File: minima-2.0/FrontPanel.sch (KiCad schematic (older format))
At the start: 41 parts

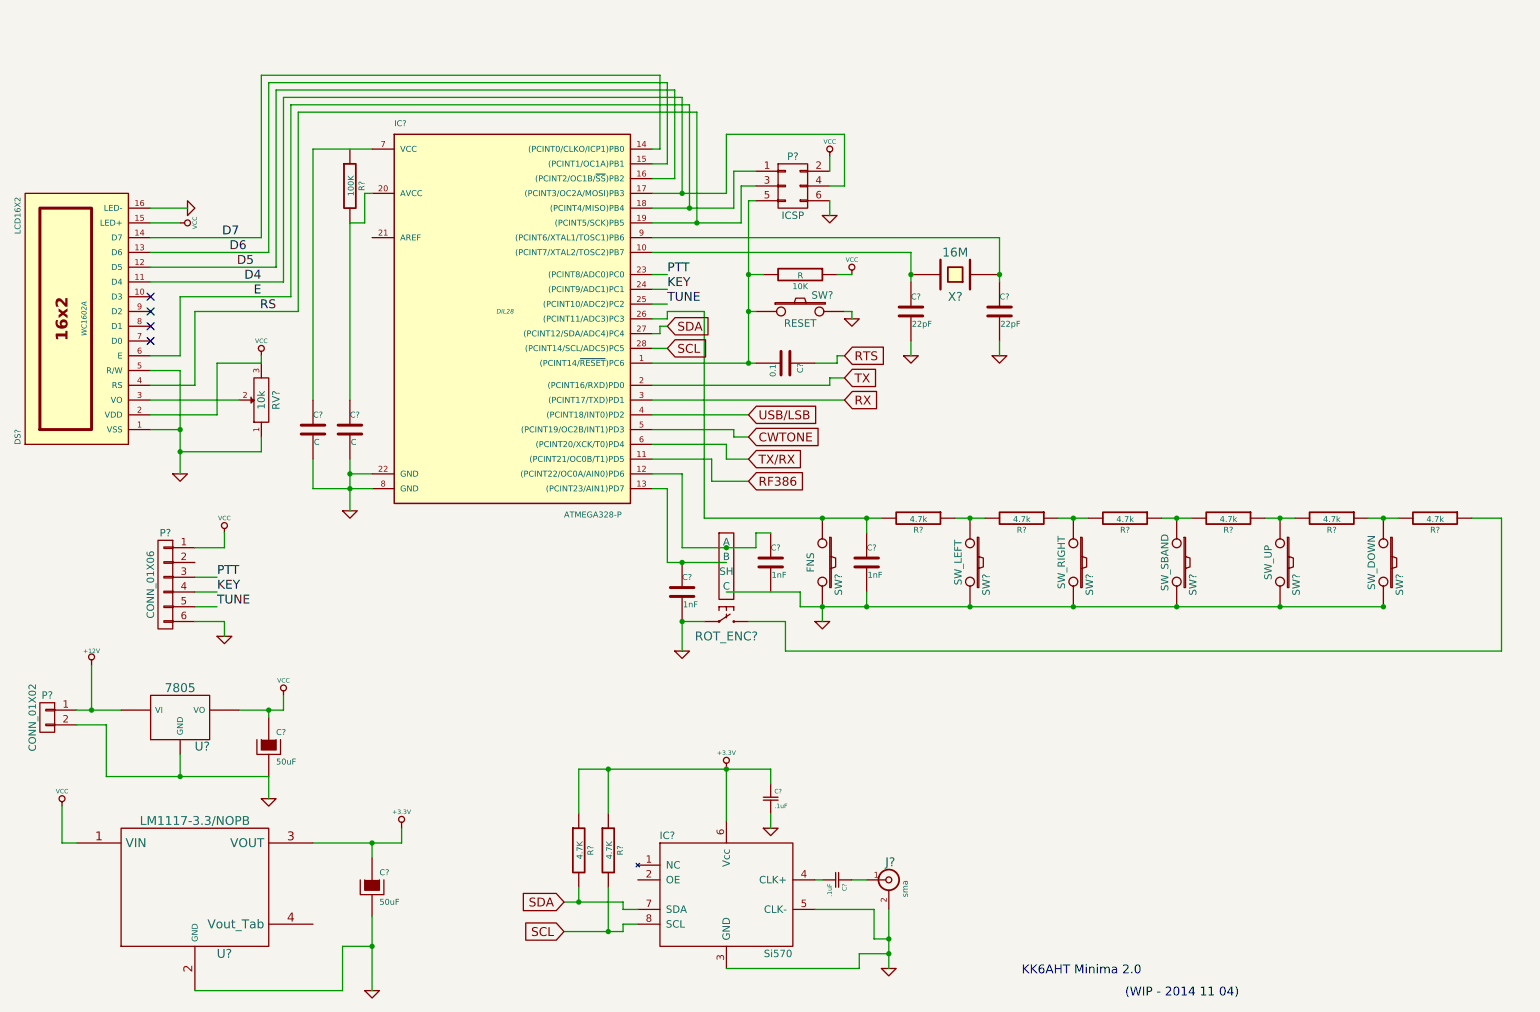
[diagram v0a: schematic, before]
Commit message: Finishing touches on schematic
 - Added missing 47k on AREF
 - Added connectors for all outside connections
 - Fixed all ERC errors
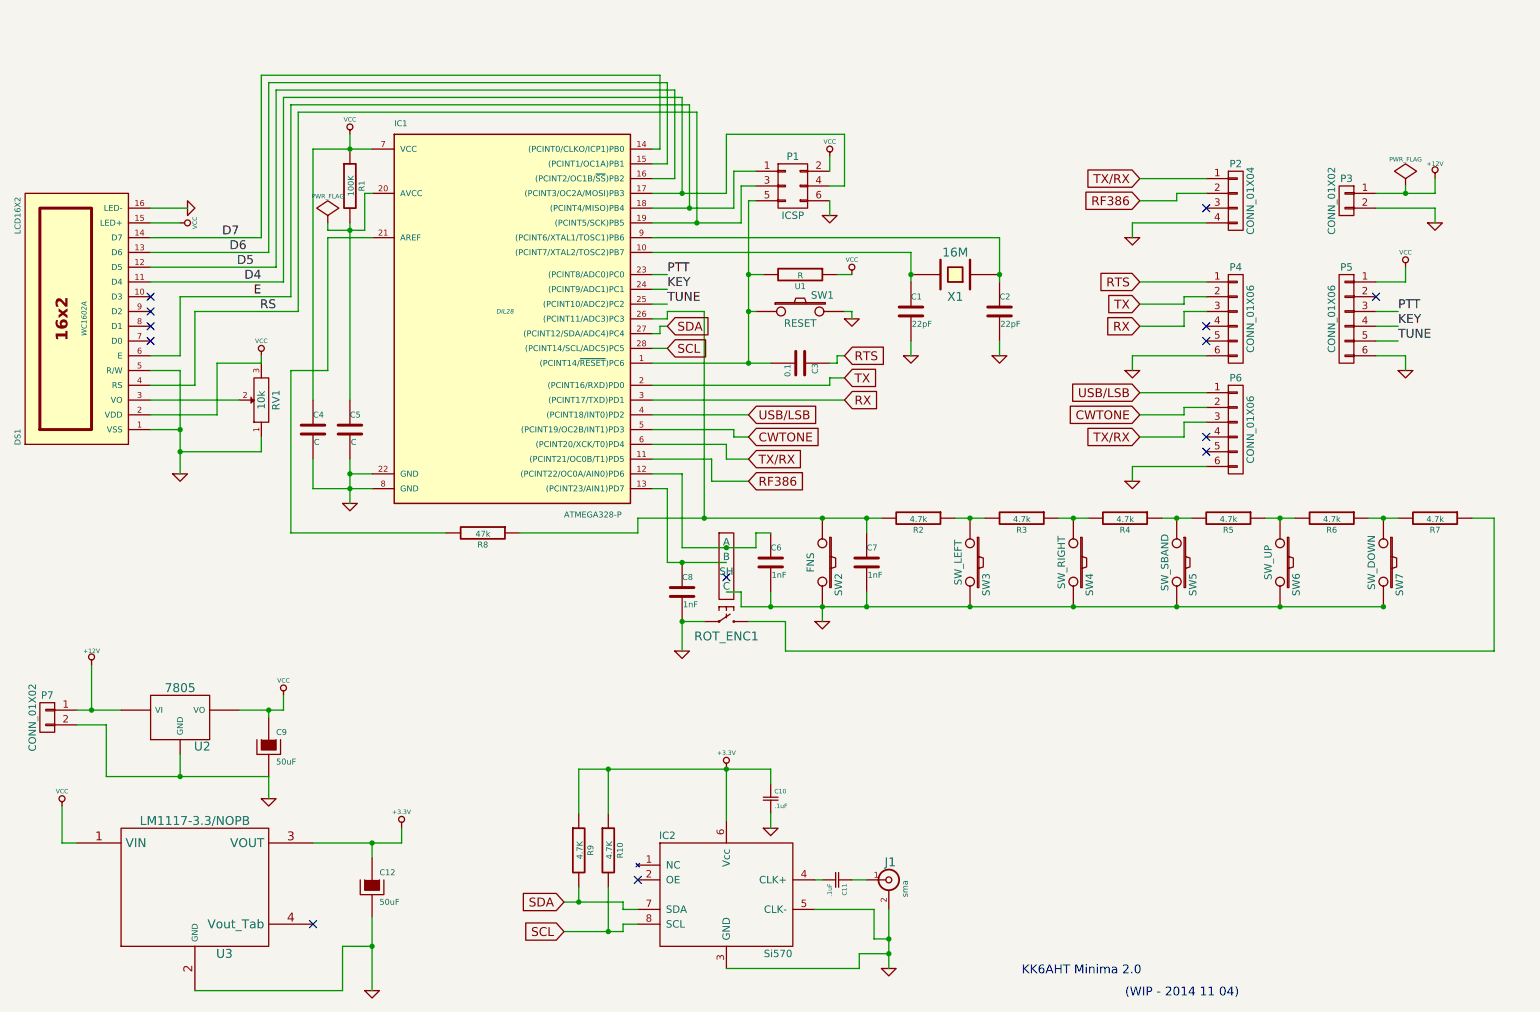
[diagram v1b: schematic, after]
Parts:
- removed J?: sma, sma, symbol sma
- removed R?: 4.7k, symbol R
- added J1: sma, sma, symbol sma
- added P2: CONN_01X04, symbol CONN_01X04
- added P3: CONN_01X02, symbol CONN_01X02
- added P4, P6: CONN_01X06, symbol CONN_01X06
- added R3: 4.7k, symbol R
- added R8: 47k, symbol R
- gave numbers to parts that had none: 38
- renumbered 10K to U1
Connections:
- net +12V: now also P3.1 (P1)
- net CWTONE: now also P6.2 (P2)
- net GND: now also C6.2, J1.2 (Ext), P2.4 (P4), P3.2 (P2), P4.6 (P6), P6.6 (P6)
- net RF386: now also P2.2 (P2)
- net RTS: now also P4.1 (P1)
- net RX: now also P4.3 (P3)
- net TX: now also P4.2 (P2)
- net TX/RX: now also P2.1 (P1), P6.3 (P3)
- net USB/LSB: now also P6.1 (P1)
- net VCC: now also C4.1, IC1.7 (VCC), R1.1
- net at IC1.21 (AREF): now also R8.2
- net at C7.1, IC1.26 ((PCINT11/ADC3)PC3), R2.2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: now also R8.1
- net at R2.1, SW3.1: now also R3.2
- net at R4.2, SW4.1: now also R3.1
- net at C11.1: now also J1.1 (In)
- no-connect marks 4 -> 13
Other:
- moved on the sheet: C3, P5

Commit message: WIP (commiting unfinished work while cleaning up laptop)
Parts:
- removed P3: CONN_01X02, symbol CONN_01X02
- removed P4, P5: CONN_01X06, symbol CONN_01X06
- removed U1: R, symbol R
- added P3, P4: CONN_01X04, Pin_Headers:Pin_Header_Angled_1x04, symbol CONN_01X04
- added R11: 10K, Discret:R4, symbol R
- added RV2: 100K, symbol POT
- C1, C10, C11, C2, C3, C4, C5, C6, C7, C8: footprint (none) -> Discret:C1
- C12, C9: footprint (none) -> Capacitors_ThroughHole:Capacitor5x6RM2.5
- DS1: footprint WC1602A -> Display:WC1602A
- IC1: footprint DIL28 -> Sockets_DIP:DIP-28__300_ELL
- IC2: footprint SI570_SI571_Standard -> Oscillators:SI570_SI571_Standard
- J1: footprint sma -> sma-edge:SMA_EDGE
- P1: footprint (none) -> Pin_Headers:Pin_Header_Straight_2x03
- P2: footprint (none) -> Pin_Headers:Pin_Header_Angled_1x04
- P5: renamed from P6; footprint (none) -> Pin_Headers:Pin_Header_Angled_1x06
- P7: footprint (none) -> Connect:bornier2
- R1, R10, R2, R3, R4, R5, R6, R7, R8, R9: footprint (none) -> Discret:R4
- ROT_ENC1: footprint (none) -> ab2_input_devices:AB2_ROTARY_ENCODER_W_SWITCH
- RV1: footprint (none) -> Potentiometers:Potentiometer_Trimmer-Suntan-TSR-3386P
- SW1, SW2, SW3, SW4, SW5, SW6, SW7: footprint (none) -> Discret:SW_PUSH_SMALL
- U2: footprint (none) -> Discret:LM78XX
- U3: footprint SOT223 -> Discret:TO220
- X1: footprint (none) -> Discret:HC-49V
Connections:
- net +3.3V: now also P3.4 (P4)
- net CWTONE: now also P5.5 (P5); no longer P5.2 (P2)
- net GND: now also P2.1 (P1), P5.1 (P1), P3.1 (P1), P4.1 (P1), RV2.1; no longer P2.4 (P4), P5.6 (P6)
- net KEY: now also P5.2 (P2)
- net PTT: now also P5.3 (P3)
- net RF386: now also P2.3 (P3); no longer P2.2 (P2)
- net RTS: now also P4.4 (P4)
- net RX: now also P4.2 (P2)
- net SCL: now also P3.2 (P2)
- net SDA: now also P3.3 (P3)
- net TUNE: now also RV2.2
- net TX: now also P4.3 (P3)
- net TX/RX: now also P2.4 (P4), P5.4 (P4); no longer P2.1 (P1), P5.3 (P3)
- net USB/LSB: now also P5.6 (P6); no longer P5.1 (P1)
- net VCC: now also R11.1, RV2.3
- net at C3.2, IC1.1 ((PCINT14/~RESET~)PC6), P1.5 (P5)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: now also R11.2
- no-connect marks 13 -> 8
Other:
- moved on the sheet: P5
